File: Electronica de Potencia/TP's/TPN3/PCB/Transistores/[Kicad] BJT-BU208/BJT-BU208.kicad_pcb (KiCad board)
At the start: 2 copper layers, 100.7 x 69.3 mm, 26 parts, among them J1 Vin, J2 PWM_IN, Q1 BC548, Q2 BC558, Q3 BU208, U1 L7812, U2 L7905

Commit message: Arreglo placa de potencia
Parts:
- moved Q2 2.52 mm to (136.1, 61.5), turned to 270 degrees
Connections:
- Q2 pad 1: Net-(D1-Pad1) -> -5V
- Q2 pad 3: -5V -> Net-(D1-Pad1)
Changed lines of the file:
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@@
     (thickness 1.6)
     (drawings 91)
-    (tracks 122)
+    (tracks 123)
     (zones 0)
     (modules 26)
@@
   )
   (module lib_fp:TO-92_Inline (layer F.Cu)
-    (at 136.144 64.008 90)
+    (at 136.125 61.485 270)
     (descr "TO-92 leads in-line, narrow, oval pads, drill 0.75mm (see NXP sot054_po.pdf)")
     (tags "to-92 sc-43 sc-43a sot54 PA33 transistor")
-    (fp_text reference Q2 (at -2.794 0 90) (layer F.SilkS)
-      (effects (font (size 1 1) (thickness 0.15)))
-    )
-    (fp_text value BC558 (at -4.318 0 270) (layer F.Fab)
+    (fp_text reference Q2 (at -2.794 0 270) (layer F.SilkS)
+      (effects (font (size 1 1) (thickness 0.15)))
+    )
+    (fp_text value BC558 (at -4.318 0 90) (layer F.Fab)
       (effects (font (size 1 1) (thickness 0.15)))
     )
@@
     (fp_line (start -0.5 1.75) (end 3 1.75) (layer F.Fab) (width 0.1))
     (fp_line (start -0.53 1.85) (end 3.07 1.85) (layer F.SilkS) (width 0.12))
-    (fp_text user %R (at 1.27 0 90) (layer F.Fab)
-      (effects (font (size 1 1) (thickness 0.15)))
-    )
-    (pad 1 thru_hole oval (at 0 0 90) (size 1.05 3) (drill 0.75) (layers *.Cu *.Mask)
+    (fp_text user %R (at 1.27 0 270) (layer F.Fab)
+      (effects (font (size 1 1) (thickness 0.15)))
+    )
+    (pad 1 thru_hole oval (at 0 0 270) (size 1.05 3) (drill 0.75) (layers *.Cu *.Mask)
+      (net 4 -5V))
+    (pad 3 thru_hole oval (at 2.54 0 270) (size 1.05 3) (drill 0.75) (layers *.Cu *.Mask)
       (net 6 "Net-(D1-Pad1)"))
-    (pad 3 thru_hole oval (at 2.54 0 90) (size 1.05 3) (drill 0.75) (layers *.Cu *.Mask)
-      (net 4 -5V))
-    (pad 2 thru_hole oval (at 1.27 0 90) (size 1.05 3) (drill 0.75) (layers *.Cu *.Mask)
+    (pad 2 thru_hole oval (at 1.27 0 270) (size 1.05 3) (drill 0.75) (layers *.Cu *.Mask)
       (net 12 "Net-(Q1-Pad2)"))
     (model ${KISYS3DMOD}/Package_TO_SOT_THT.3dshapes/TO-92_Inline.wrl
@@
   (segment (start 95.8215 64.0715) (end 95.758 64.008) (width 2) (layer B.Cu) (net 3) (status 30))
   (segment (start 95.8215 73.5965) (end 95.8215 64.0715) (width 2) (layer B.Cu) (net 3) (status 30))
-  (segment (start 95.8215 77.3557) (end 95.8215 73.5965) (width 2) (layer B.Cu) (net 3))
-  (segment (start 83.566 80.264) (end 92.9132 80.264) (width 2) (layer B.Cu) (net 3))
+  (segment (start 95.8215 77.3557) (end 95.8215 73.5965) (width 2) (layer B.Cu) (net 3) (status 20))
+  (segment (start 83.566 80.264) (end 92.9132 80.264) (width 2) (layer B.Cu) (net 3) (status 10))
   (segment (start 92.9132 80.264) (end 95.8215 77.3557) (width 2) (layer B.Cu) (net 3))
   (segment (start 121.698 62.262) (end 119.126 62.262) (width 1) (layer B.Cu) (net 4) (status 20))
@@
   (segment (start 119.126 55.118) (end 119.126 62.262) (width 1) (layer B.Cu) (net 4) (status 20))
   (segment (start 123.19 51.054) (end 119.126 55.118) (width 1) (layer B.Cu) (net 4))
-  (segment (start 135.636 51.054) (end 128.778 51.054) (width 1) (layer B.Cu) (net 4))
-  (segment (start 139.4968 61.468) (end 142.6972 58.2676) (width 1) (layer B.Cu) (net 4))
-  (segment (start 136.144 61.468) (end 139.4968 61.468) (width 1) (layer B.Cu) (net 4))
-  (segment (start 142.6972 58.2676) (end 142.6972 54.9656) (width 1) (layer B.Cu) (net 4))
-  (segment (start 142.6972 54.9656) (end 141.3256 53.594) (width 1) (layer B.Cu) (net 4))
-  (segment (start 141.3256 53.594) (end 138.176 53.594) (width 1) (layer B.Cu) (net 4))
-  (segment (start 138.176 53.594) (end 135.636 51.054) (width 1) (layer B.Cu) (net 4))
+  (segment (start 139.4798 61.485) (end 136.125 61.485) (width 1) (layer B.Cu) (net 4))
+  (segment (start 135.636 51.054) (end 138.176 53.594) (width 1) (layer B.Cu) (net 4))
+  (segment (start 128.778 51.054) (end 135.636 51.054) (width 1) (layer B.Cu) (net 4))
+  (segment (start 138.176 53.594) (end 141.3256 53.594) (width 1) (layer B.Cu) (net 4))
+  (segment (start 141.3256 53.594) (end 142.6972 54.9656) (width 1) (layer B.Cu) (net 4))
+  (segment (start 142.6972 54.9656) (end 142.6972 58.2676) (width 1) (layer B.Cu) (net 4))
+  (segment (start 142.6972 58.2676) (end 139.4798 61.485) (width 1) (layer B.Cu) (net 4))
   (segment (start 113.792 87.376) (end 105.918 87.376) (width 1) (layer B.Cu) (net 5) (status 10))
   (segment (start 105.918 87.376) (end 98.552 87.376) (width 1) (layer B.Cu) (net 5) (status 20))
   (segment (start 131.064 57.984) (end 126.746 62.302) (width 1) (layer B.Cu) (net 5))
-  (segment (start 131.064 56.134) (end 131.064 57.984) (width 1) (layer B.Cu) (net 5))
+  (segment (start 131.064 56.134) (end 131.064 57.984) (width 1) (layer B.Cu) (net 5) (status 10))
   (segment (start 126.746 62.302) (end 126.746 73.406) (width 1) (layer B.Cu) (net 5))
   (segment (start 126.746 73.406) (end 123.19 76.962) (width 1) (layer B.Cu) (net 5))
-  (segment (start 98.552 82.4992) (end 98.552 87.376) (width 1) (layer B.Cu) (net 5))
+  (segment (start 98.552 82.4992) (end 98.552 87.376) (width 1) (layer B.Cu) (net 5) (status 20))
   (segment (start 123.19 76.962) (end 104.0892 76.962) (width 1) (layer B.Cu) (net 5))
   (segment (start 104.0892 76.962) (end 98.552 82.4992) (width 1) (layer B.Cu) (net 5))
@@
   (segment (start 130.624 88.714) (end 131.9022 89.9922) (width 1) (layer B.Cu) (net 6))
   (segment (start 131.4704 87.376) (end 130.624 87.376) (width 1) (layer B.Cu) (net 6))
-  (segment (start 136.144 64.008) (end 136.144 82.7024) (width 1) (layer B.Cu) (net 6) (status 10))
   (segment (start 136.144 82.7024) (end 131.4704 87.376) (width 1) (layer B.Cu) (net 6))
   (segment (start 160.346 56.134) (end 160.6 55.88) (width 1) (layer B.Cu) (net 6) (status 30))
@@
   (segment (start 139.954 56.134) (end 147.2184 56.134) (width 1) (layer F.Cu) (net 6))
   (segment (start 147.2184 56.134) (end 147.4216 55.9308) (width 1) (layer F.Cu) (net 6))
-  (segment (start 160.7312 55.9308) (end 160.782 55.88) (width 1) (layer B.Cu) (net 6))
-  (segment (start 147.4216 55.9308) (end 160.7312 55.9308) (width 1) (layer B.Cu) (net 6))
-  (segment (start 137.894 64.008) (end 136.144 64.008) (width 1) (layer B.Cu) (net 6))
-  (segment (start 143.764 64.008) (end 137.894 64.008) (width 1) (layer B.Cu) (net 6))
+  (segment (start 160.7312 55.9308) (end 160.782 55.88) (width 1) (layer B.Cu) (net 6) (status 30))
+  (segment (start 147.4216 55.9308) (end 160.7312 55.9308) (width 1) (layer B.Cu) (net 6) (status 20))
+  (segment (start 136.142 64.008) (end 136.125 64.025) (width 1) (layer B.Cu) (net 6))
+  (segment (start 143.764 64.008) (end 136.142 64.008) (width 1) (layer B.Cu) (net 6))
   (segment (start 147.4216 55.9308) (end 147.4216 60.3504) (width 1) (layer B.Cu) (net 6))
   (segment (start 147.4216 60.3504) (end 143.764 64.008) (width 1) (layer B.Cu) (net 6))
+  (segment (start 136.125 82.6834) (end 136.144 82.7024) (width 1) (layer B.Cu) (net 6))
+  (segment (start 136.125 64.025) (end 136.125 82.6834) (width 1) (layer B.Cu) (net 6))
   (segment (start 88.392 91.948) (end 88.392 87.376) (width 1) (layer B.Cu) (net 7) (status 30))
   (segment (start 100.652 91.948) (end 98.552 91.948) (width 1) (layer B.Cu) (net 8) (status 20))
@@
   (segment (start 120.142 84.074) (end 127.762 84.074) (width 1) (layer B.Cu) (net 12))
   (segment (start 127.762 84.074) (end 133.604 78.232) (width 1) (layer B.Cu) (net 12))
-  (segment (start 137.894 62.738) (end 136.144 62.738) (width 1) (layer B.Cu) (net 12))
+  (segment (start 137.894 62.738) (end 136.144 62.738) (width 1) (layer B.Cu) (net 12) (status 20))
   (segment (start 141.662 62.738) (end 137.894 62.738) (width 1) (layer B.Cu) (net 12))
   (segment (start 144.4244 59.9756) (end 141.662 62.738) (width 1) (layer B.Cu) (net 12))
   (segment (start 144.4244 54.102) (end 144.4244 59.9756) (width 1) (layer B.Cu) (net 12))
-  (segment (start 138.938 51.054) (end 141.3764 51.054) (width 1) (layer B.Cu) (net 12))
+  (segment (start 138.938 51.054) (end 141.3764 51.054) (width 1) (layer B.Cu) (net 12) (status 10))
   (segment (start 141.3764 51.054) (end 144.4244 54.102) (width 1) (layer B.Cu) (net 12))
-  (segment (start 104.9528 79.1972) (end 103.886 80.264) (width 1) (layer B.Cu) (net 13))
-  (segment (start 125.2728 79.1972) (end 104.9528 79.1972) (width 1) (layer B.Cu) (net 13))
-  (segment (start 130.81 64.008) (end 130.81 73.66) (width 1) (layer B.Cu) (net 13))
+  (segment (start 104.9528 79.1972) (end 103.886 80.264) (width 1) (layer B.Cu) (net 13) (status 30))
+  (segment (start 125.2728 79.1972) (end 104.9528 79.1972) (width 1) (layer B.Cu) (net 13) (status 20))
+  (segment (start 130.81 64.008) (end 130.81 73.66) (width 1) (layer B.Cu) (net 13) (status 10))
   (segment (start 130.81 73.66) (end 125.2728 79.1972) (width 1) (layer B.Cu) (net 13))
   (zone (net 2) (net_name GND) (layer B.Cu) (hatch edge 0.508)

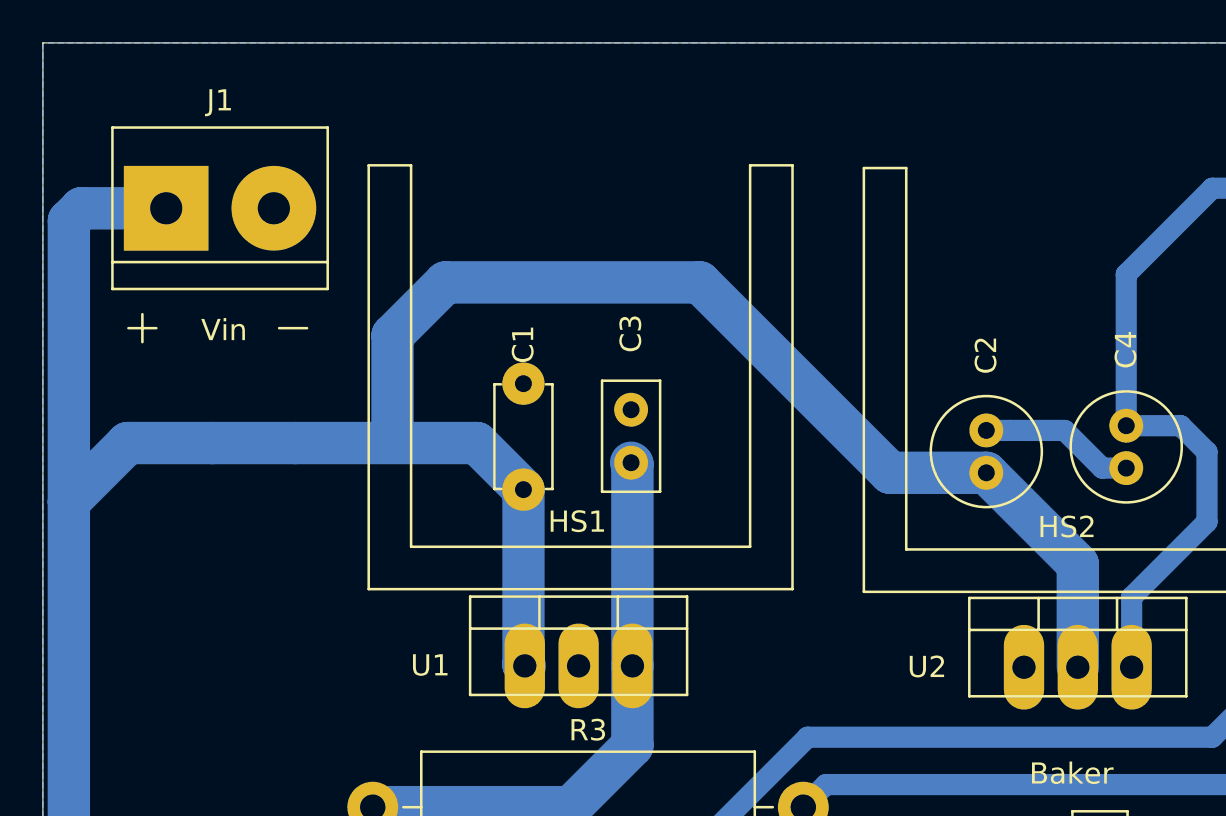
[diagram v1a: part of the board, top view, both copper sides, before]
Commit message: Arreglo placa BJT potencia
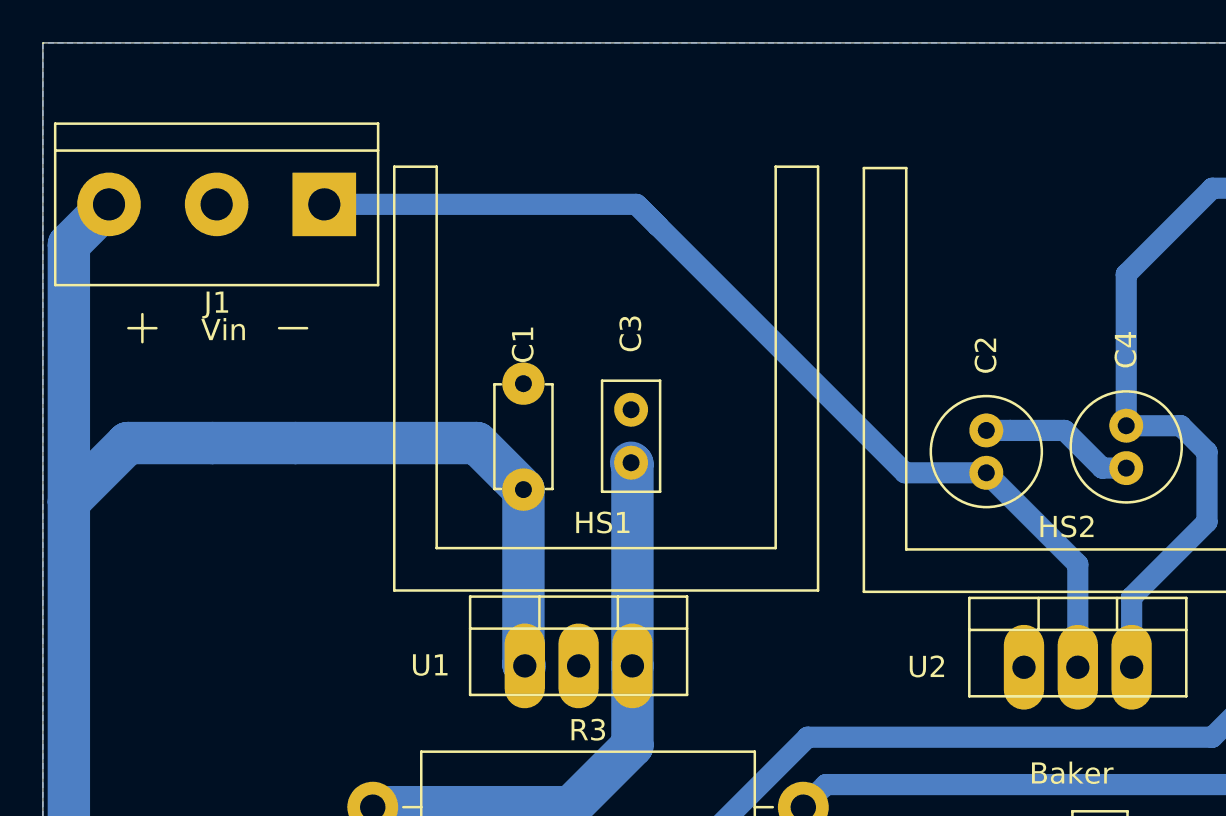
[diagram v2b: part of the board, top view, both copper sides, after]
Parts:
- J1: value Vin -> Conn_01x03; footprint lib_fp:TerminalBlock_bornier-2_P5.08mm -> lib_fp:TerminalBlock_bornier-3_P5.08mm
- moved J1 7.46 mm to (81.3, 51.8), turned to 180 degrees
- moved HS1 1.21 mm to (84.6, 50.0)
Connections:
- C2 pad 2: +15V -> -15V
- J1 pad 1: +15V -> -15V
- U2 pad 2: +15V -> -15V
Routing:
- net +15V: track 137.6 -> 85.5 mm
- net -15V: track 0.00 -> 48.7 mm
